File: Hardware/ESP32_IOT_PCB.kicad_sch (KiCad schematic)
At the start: 0 parts

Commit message: Major Updates to Schematic
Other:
- sheet Digital Bus ports: added SCL, SDA; removed +3V3, GND
- sheet MCU and Power ports: added 1.8V, SCL, SDA; removed +3V3, GND
- sheet UI and Outputs ports: added none; removed GND
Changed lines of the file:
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@@
 		(title "ESP32 Sensor Board")
-	)
-	(junction
-		(at 180.34 115.57)
-		(diameter 0)
-		(color 0 0 0 0)
-	)
-	(wire
-		(pts
-			(xy 180.34 115.57) (xy 191.77 115.57)
-		)
-		(stroke
-			(width 0)
-			(type default)
-		)
-	)
-	(wire
-		(pts
-			(xy 170.18 78.74) (xy 180.34 78.74)
-		)
-		(stroke
-			(width 0)
-			(type default)
-		)
-	)
-	(wire
-		(pts
-			(xy 170.18 115.57) (xy 180.34 115.57)
-		)
-		(stroke
-			(width 0)
-			(type default)
-		)
-	)
-	(wire
-		(pts
-			(xy 170.18 101.6) (xy 191.77 101.6)
-		)
-		(stroke
-			(width 0)
-			(type default)
-		)
-	)
-	(wire
-		(pts
-			(xy 180.34 78.74) (xy 180.34 115.57)
-		)
-		(stroke
-			(width 0)
-			(type default)
-		)
 	)
 	(sheet
@@
 			)
 		)
-		(pin "+3V3" input
-			(at 191.77 101.6 180)
+		(pin "SCL" bidirectional
+			(at 191.77 96.52 90)
 			(effects
 				(font
 					(size 1.27 1.27)
 				)
-				(justify left)
+				(justify right)
 			)
 		)
-		(pin "GND" input
-			(at 191.77 115.57 180)
+		(pin "SDA" bidirectional
+			(at 193.3893 96.52 90)
 			(effects
 				(font
 					(size 1.27 1.27)
 				)
-				(justify left)
+				(justify right)
 			)
 		)
@@
 			)
 		)
-		(pin "+3V3" output
-			(at 170.18 101.6 0)
+		(pin "1.8V" output
+			(at 139.7 96.52 90)
 			(effects
 				(font
 					(size 1.27 1.27)
-					(color 0 0 0 1)
 				)
 				(justify right)
 			)
 		)
-		(pin "GND" output
-			(at 170.18 115.57 0)
+		(pin "SCL" bidirectional
+			(at 141.3193 96.52 90)
+			(effects
+				(font
+					(size 1.27 1.27)
+				)
+				(justify right)
+			)
+		)
+		(pin "SDA" bidirectional
+			(at 142.9386 96.52 90)
 			(effects
 				(font
@@
 			)
 		)
-		(pin "GND" input
-			(at 170.18 78.74 0)
-			(effects
-				(font
-					(size 1.27 1.27)
-				)
-				(justify right)
-			)
-		)

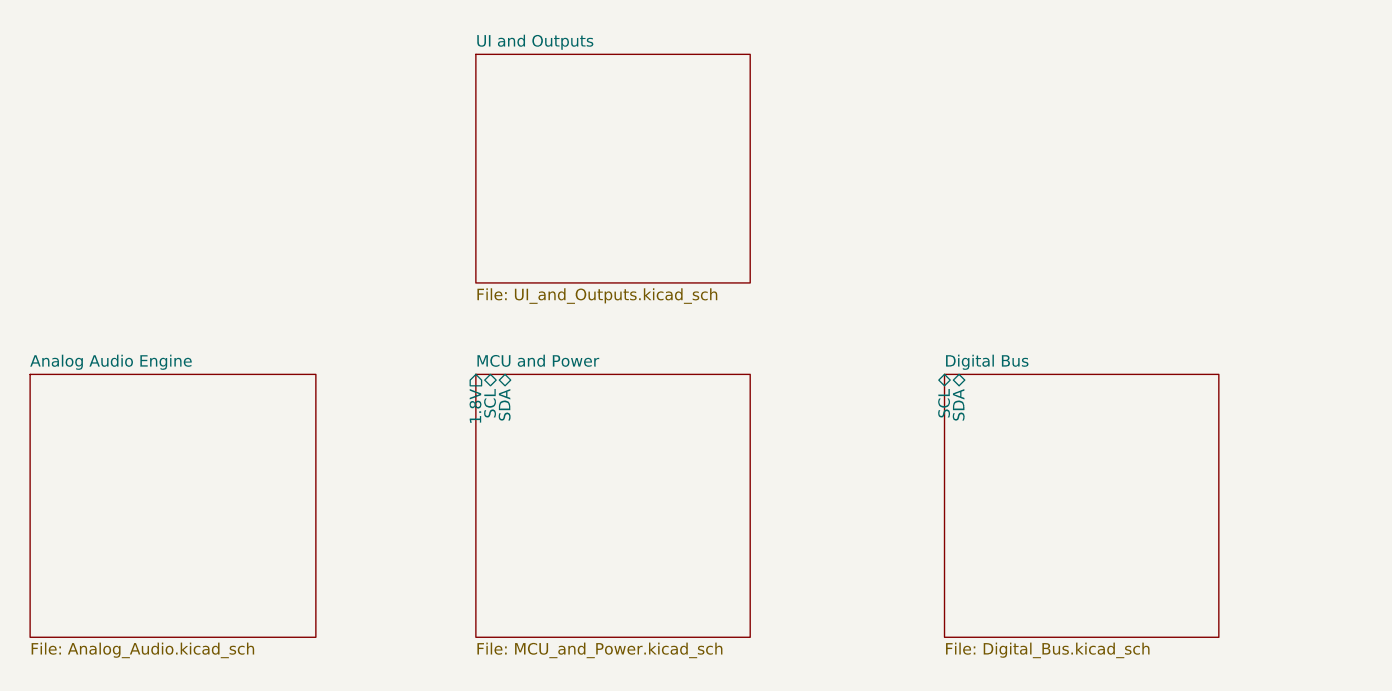
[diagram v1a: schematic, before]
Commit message: Schematic V0.9 is complete
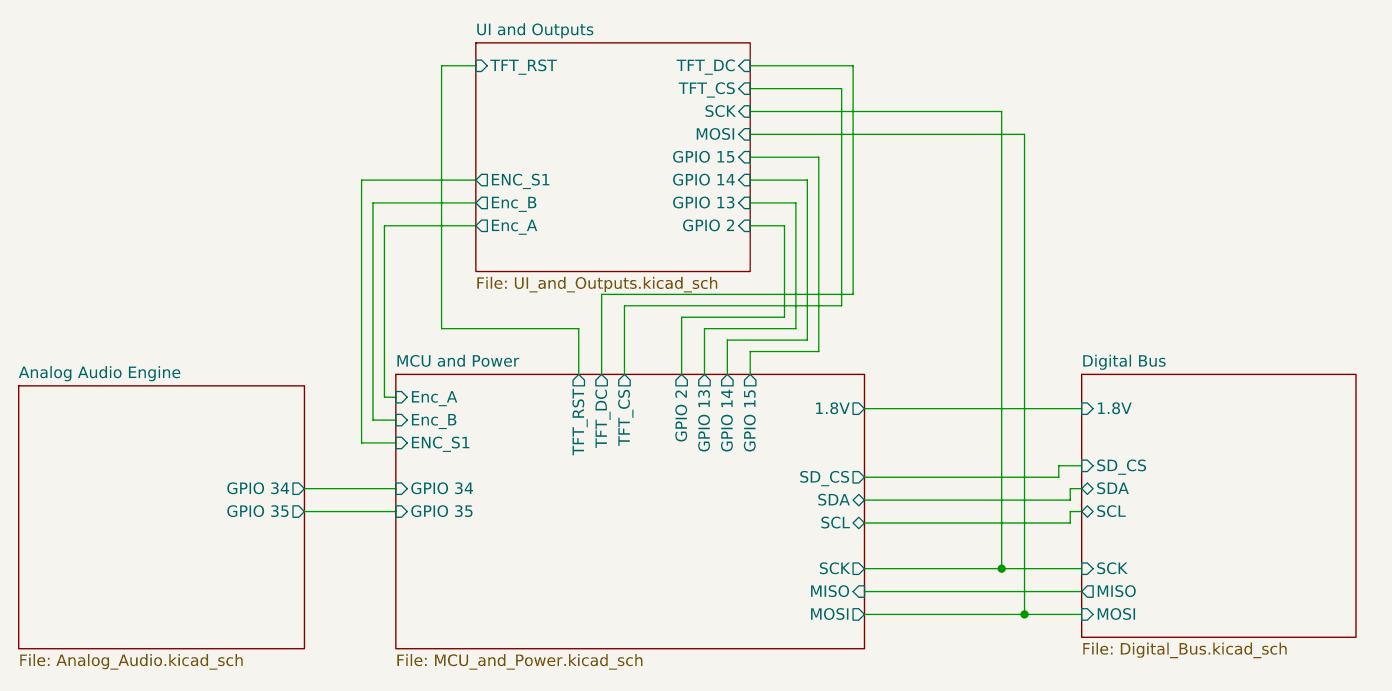
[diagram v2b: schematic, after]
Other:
- sheet Analog Audio Engine ports: added GPIO 34, GPIO 35; removed none
- sheet Digital Bus ports: added 1.8V, MISO, MOSI, SCK, SD_CS; removed none
- sheet MCU and Power ports: added ENC_S1, Enc_A, Enc_B, GPIO 13, GPIO 14, GPIO 15, GPIO 2, GPIO 34, GPIO 35, MISO, MOSI, SCK, SD_CS, TFT_CS, TFT_DC, TFT_RST; removed none
- sheet UI and Outputs ports: added ENC_S1, Enc_A, Enc_B, GPIO 13, GPIO 14, GPIO 15, GPIO 2, MOSI, SCK, TFT_CS, TFT_DC, TFT_RST; removed none
